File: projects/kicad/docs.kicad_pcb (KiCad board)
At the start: 2 copper layers, 2 parts

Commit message: Update_0122
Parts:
- added D1: D, kbd_parts:D_SOD-123-Pretty, F.Cu at (223.8, 55.4)
- added D2: D, kbd_parts:D_SOD-123-Pretty, F.Cu at (223.8, 58.8)
- added D3: D, kbd_parts:D_SOD-123-Pretty, F.Cu at (223.8, 62.1)
- added D4: D, kbd_parts:D_SOD-123-Pretty, F.Cu at (223.8, 65.5)
- added D5: D, kbd_parts:D_SOD-123-Pretty, F.Cu at (223.8, 68.8)
- added D6: D, kbd_parts:D_SOD-123-Pretty, F.Cu at (223.8, 72.2)
- added D7: D, kbd_parts:D_SOD-123-Pretty, F.Cu at (223.8, 75.5)
- added SW1: SW_PUSH, kbd:keyswitch_choc12_gateron_low_profile_hotswap_1u_no_led, F.Cu at (188.4, 44.1)
- added SW2: SW_PUSH, kbd:keyswitch_choc12_gateron_low_profile_hotswap_1u_no_led, F.Cu at (188.4, 53.4)
- added SW3: SW_PUSH, kbd:keyswitch_choc12_gateron_low_profile_hotswap_1u_no_led, F.Cu at (188.4, 62.7)
- added SW4: SW_PUSH, kbd:keyswitch_choc12_gateron_low_profile_hotswap_1u_no_led, F.Cu at (188.4, 72.0)
- added SW5: SW_PUSH, kbd:keyswitch_choc12_gateron_low_profile_hotswap_1u_no_led, F.Cu at (188.4, 81.2)
- added SW6: SW_PUSH, kbd:keyswitch_choc12_gateron_low_profile_hotswap_1u_no_led, F.Cu at (188.4, 90.5)
- added SW7: RotaryEncoder_Switch, Rotary_Encoder:RotaryEncoder_Bourns_Vertical_PEC12R-3x17F-Sxxxx, F.Cu at (186.5, 119.5)
- added U2: LCD, ST7789v_Library:ST7789V, F.Cu at (98.8, 109.3)

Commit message: chocolate: Update_0126
とりあえず部品の配置。
配線はまだ手つけてないです。。
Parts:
- removed the REF** at (126.0, 46.5)
- added D10: LED, kbd:LED_WS2812B-PLCC4, F.Cu at (186.0, 108.0)
- added D8: LED, kbd:LED_WS2812B-PLCC4, F.Cu at (167.0, 108.0)
- added D9: LED, kbd:LED_WS2812B-PLCC4, F.Cu at (176.5, 108.0)
- D1, D2, D3, D4, D5, D6, D7, SW1, SW2, SW3, SW4, SW5, SW6, SW7: moved to B.Cu
- moved D2 129.5 mm to (105.3, 111.0), turned to 180 degrees
- moved D1 119.8 mm to (105.0, 70.5), turned to 180 degrees
- moved D4 109.3 mm to (124.5, 111.0), turned to 180 degrees
- moved D3 99.9 mm to (124.3, 70.5), turned to 180 degrees
- moved SW2 95.4 mm to (105.3, 100.2), turned to 180 degrees
- moved REF** 93.7 mm to (176.1, 51.9)
- moved SW1 91.0 mm to (105.2, 81.0), turned to 180 degrees
- moved D6 88.8 mm to (144.0, 111.0), turned to 180 degrees
- moved D5 80.1 mm to (143.8, 70.5), turned to 180 degrees
- moved U2 73.2 mm to (92.5, 36.3)
- moved SW4 70.0 mm to (124.4, 100.2), turned to 180 degrees
- moved SW3 66.6 mm to (124.4, 81.0), turned to 180 degrees
- moved D7 53.3 mm to (176.2, 99.5), turned to 180 degrees
- moved SW6 46.0 mm to (143.5, 100.2), turned to 180 degrees
- moved SW5 44.9 mm to (143.5, 81.0), turned to 180 degrees
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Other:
- board outline added: 107 x 89.5 mm

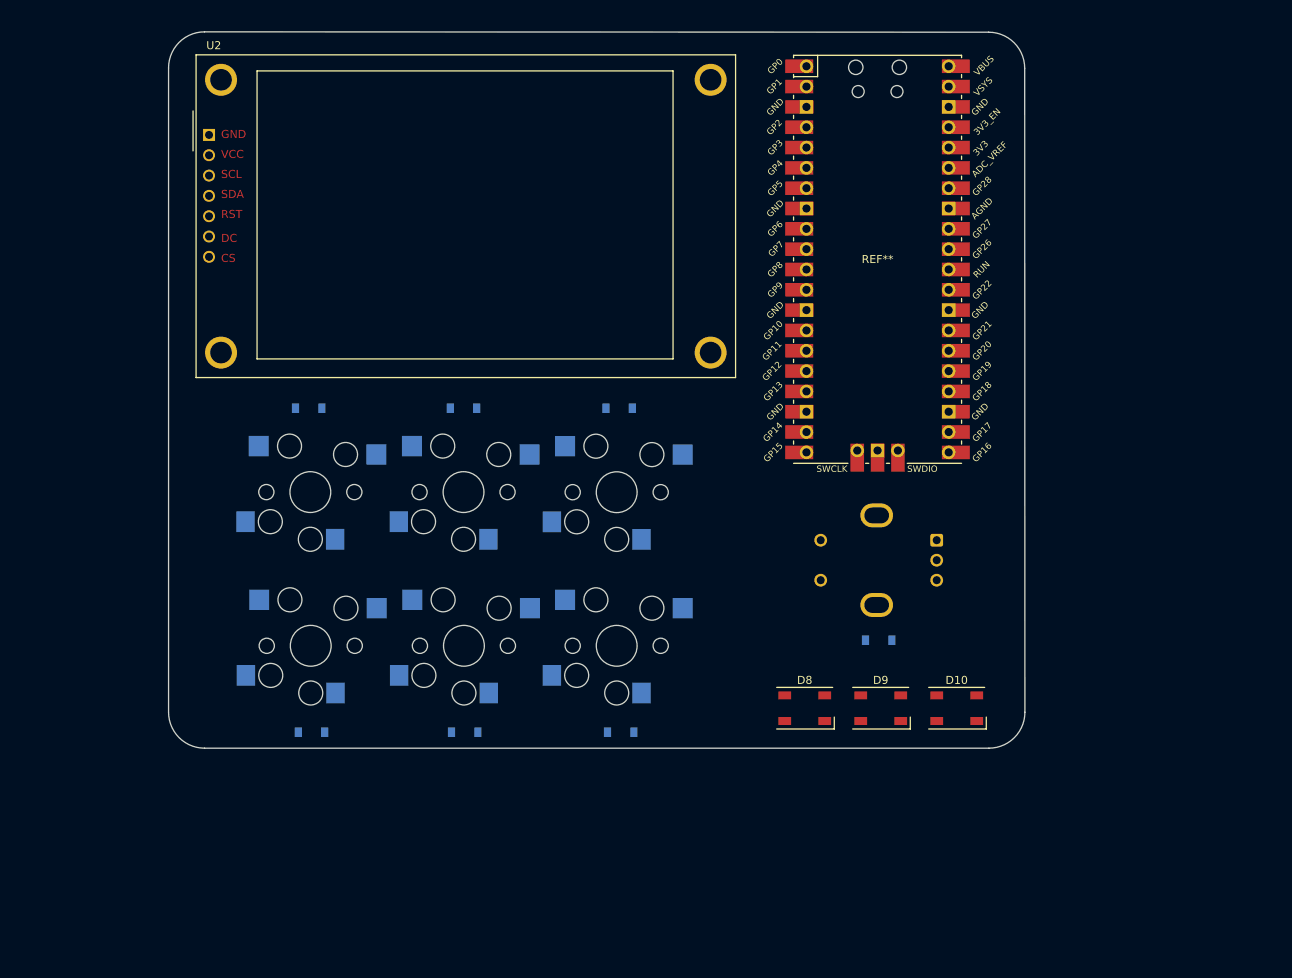
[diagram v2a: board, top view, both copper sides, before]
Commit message: chocolate: Update_0126
TFTディスプレイ 240x320 追加
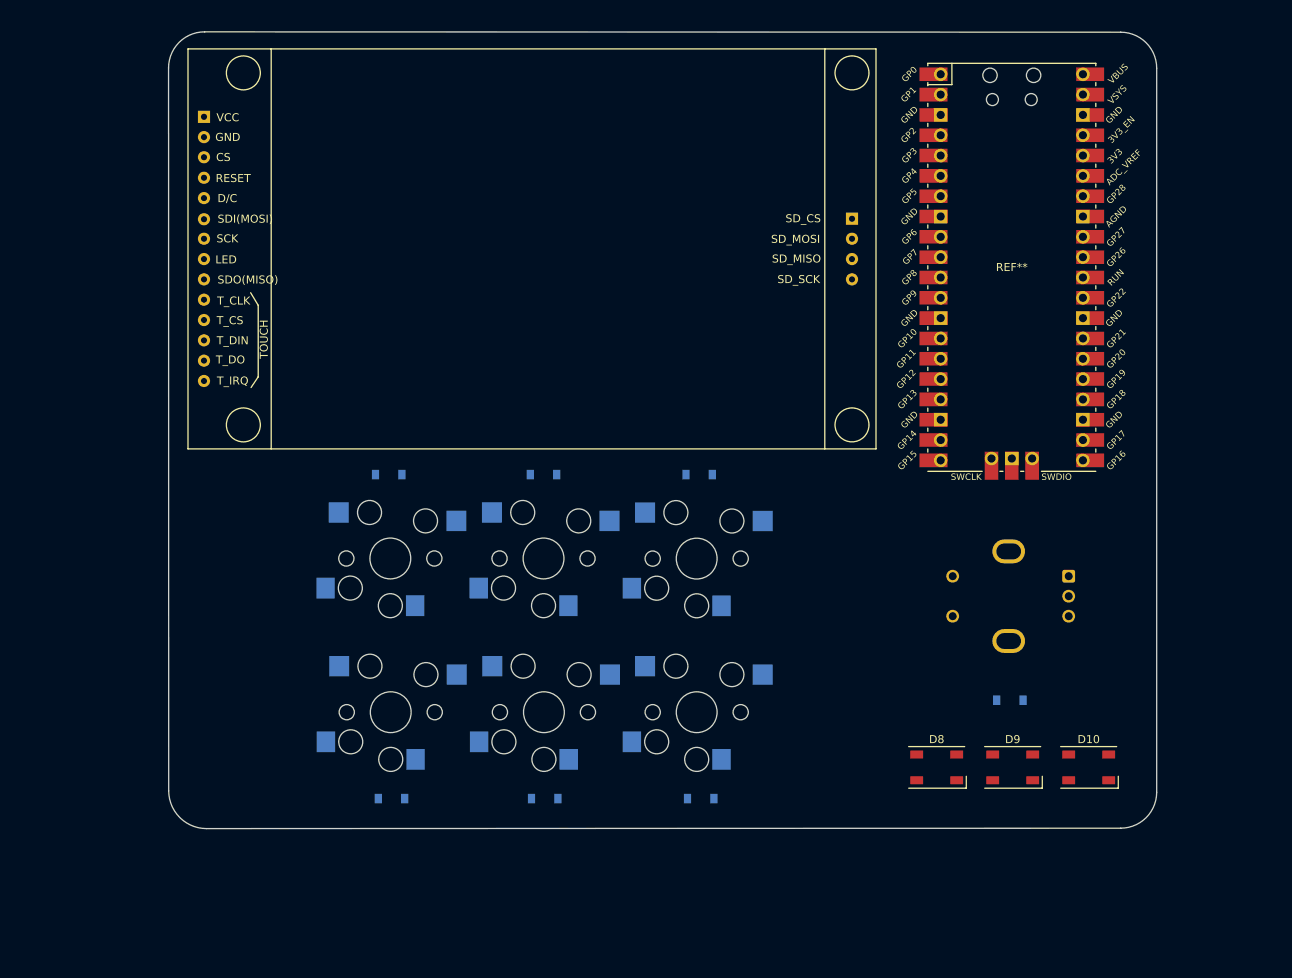
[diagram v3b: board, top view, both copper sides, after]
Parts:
- U2: footprint ST7789v_Library:ST7789V -> tft_displays:2.8_tft_240x320_touch_sd_spi
- moved U2 84.1 mm to (175.9, 25.6), turned to -90 degrees
- moved D10 18.1 mm to (202.5, 115.4)
- moved D8 18.1 mm to (183.5, 115.4)
- moved D9 18.1 mm to (193.0, 115.4)
- moved D7 18.0 mm to (192.7, 107.0)
- moved SW7 17.1 mm to (200.0, 91.5)
- moved REF** 16.8 mm to (192.9, 52.9)
- moved D1 13.0 mm to (115.0, 78.8)
- moved D2 13.0 mm to (115.3, 119.3)
- moved D3 13.0 mm to (134.3, 78.8)
- moved D4 13.0 mm to (134.5, 119.3)
- moved D5 13.0 mm to (153.8, 78.8)
- moved D6 13.0 mm to (154.0, 119.3)
- moved SW1 13.0 mm to (115.2, 89.3)
- moved SW2 13.0 mm to (115.3, 108.5)
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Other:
- board size 107 x 89.5 mm -> 123.5 x 99.6 mm

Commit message: Update_0128
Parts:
- removed REF**: RPi_Pico_SMD_TH, KiCAD_RP_Pico:RPi_Pico_SMD_TH
- removed U2: LCD, tft_displays:2.8_tft_240x320_touch_sd_spi
- added U1: Pico, KiCad-RP-Pico-main:RPi_Pico_SMD_TH, F.Cu at (149.4, 39.4)
- added U3: 2.8_240x320_touch_sd_spi, original_tft_display:2.8_tft_240x320_touch_sd_spi, F.Cu at (176.0, 24.0)
- moved D10 33.4 mm to (170.0, 107.5)
- moved D9 32.0 mm to (162.0, 107.5)
- moved D7 31.2 mm to (161.9, 101.5)
- moved SW7 31.2 mm to (169.2, 86.0)
- moved D8 30.5 mm to (154.0, 107.5)
- moved D1 16.0 mm to (99.0, 78.0)
- moved D2 16.0 mm to (99.3, 118.5)
- moved D3 16.0 mm to (118.3, 78.0)
- moved D4 16.0 mm to (118.5, 118.5)
- moved D5 16.0 mm to (137.8, 78.0)
- moved D6 16.0 mm to (138.0, 118.5)
- moved SW1 16.0 mm to (99.2, 88.5)
- moved SW2 16.0 mm to (99.3, 107.7)
- moved SW3 16.0 mm to (118.4, 88.5)
- moved SW4 16.0 mm to (118.4, 107.7)
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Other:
- board size 123.5 x 99.6 mm -> 96.5 x 103.5 mm

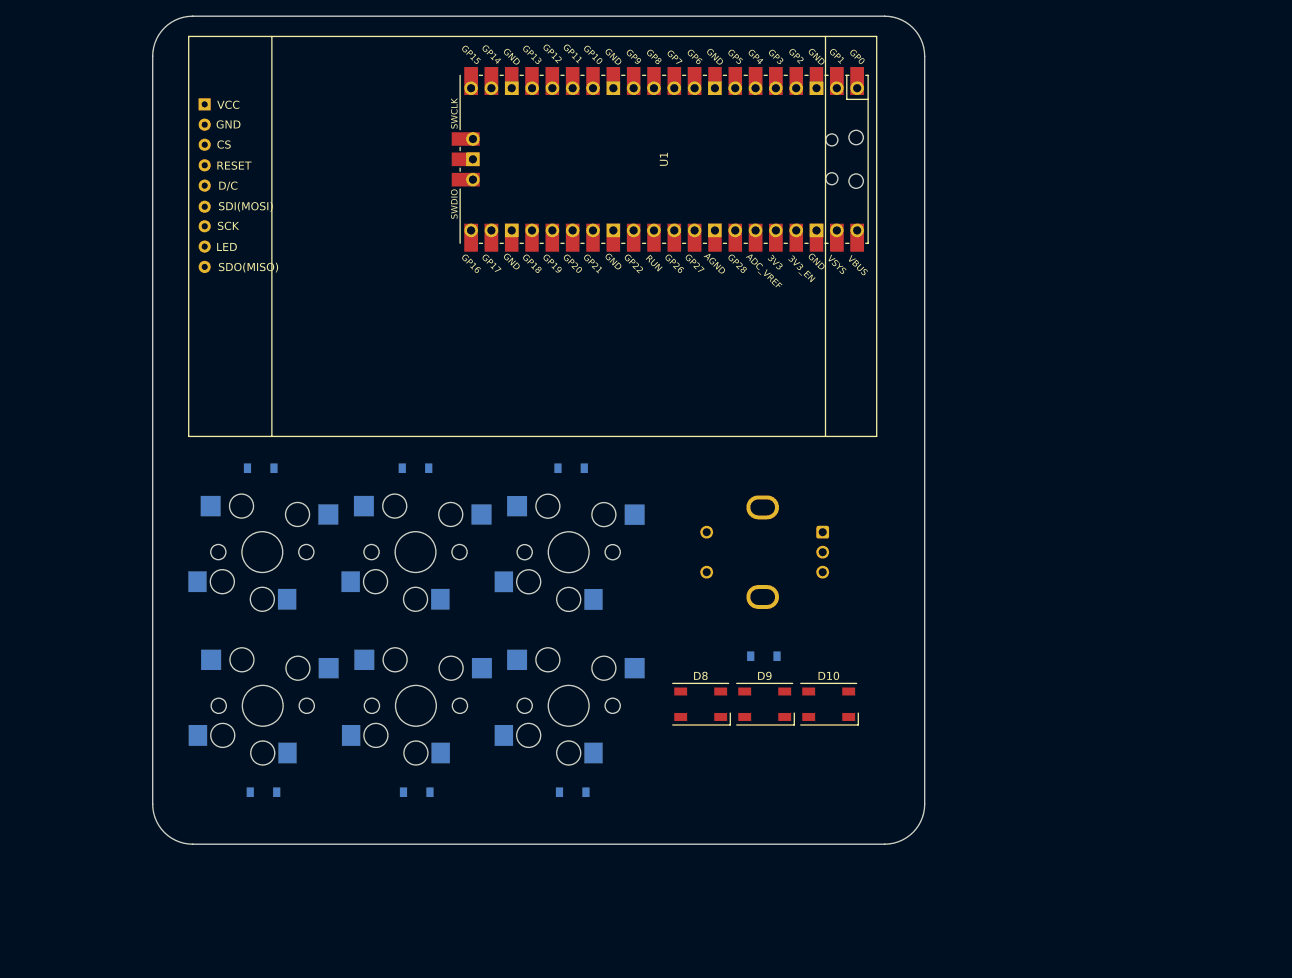
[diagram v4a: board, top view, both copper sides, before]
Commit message: chocolate: Update 01_29
配線を実施。
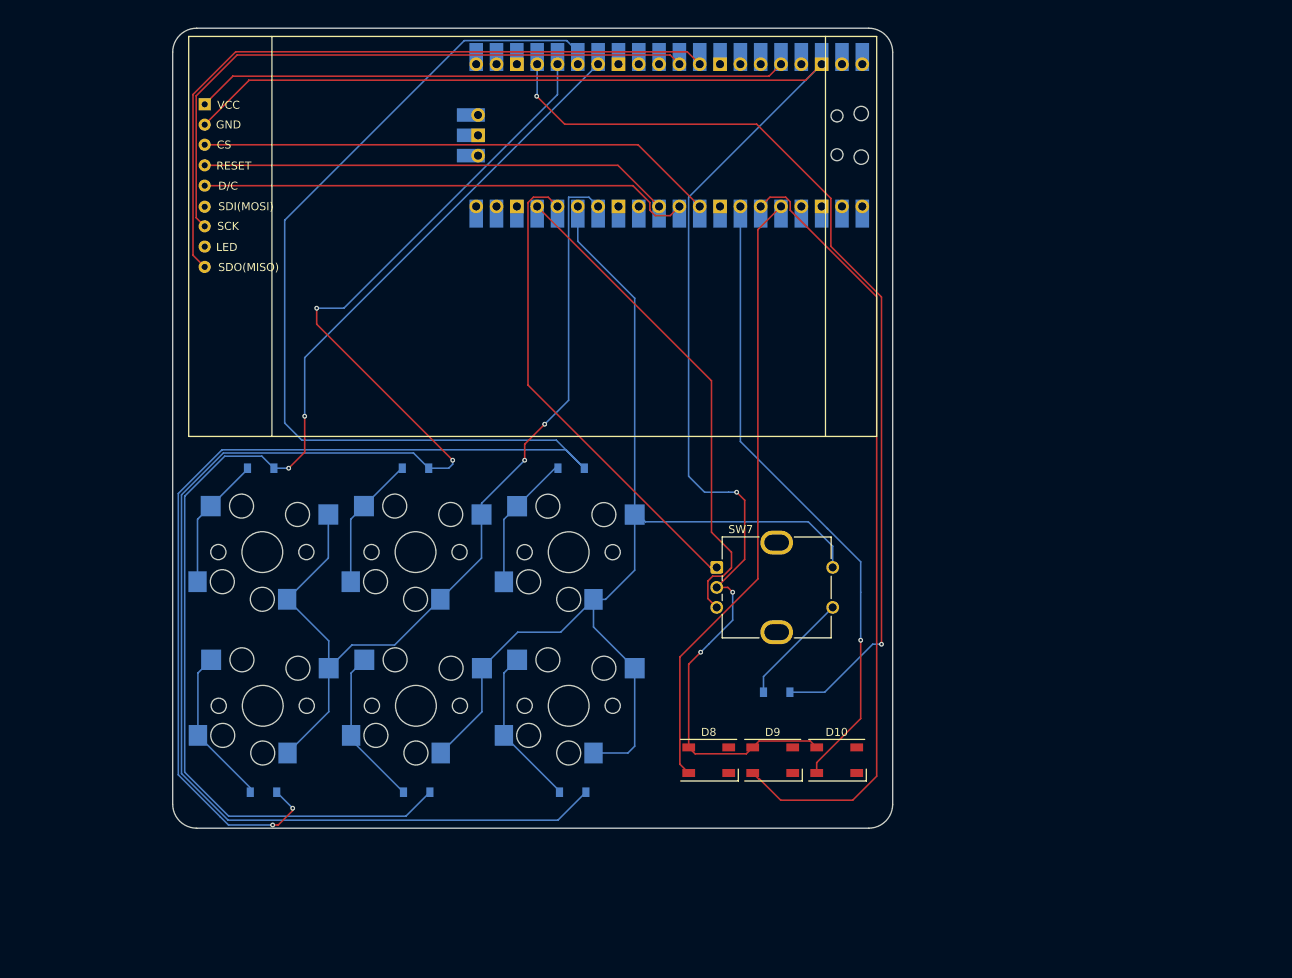
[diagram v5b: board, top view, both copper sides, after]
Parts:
- SW7: moved to F.Cu
- U1: moved to B.Cu
- moved SW7 14.0 mm to (156.0, 90.4), turned to 0 degrees
- moved D10 7.07 mm to (171.0, 114.5)
- moved D8 7.07 mm to (155.0, 114.5)
- moved D9 7.07 mm to (163.0, 114.5)
- moved D7 4.78 mm to (163.5, 106.0)
- moved U1 3.07 mm to (150.1, 36.4), turned to 90 degrees
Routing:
- net Row1: track 0.00 -> 223.1 mm, vias 0 -> 2
- net GND: track 0.00 -> 200.5 mm, vias 0 -> 3
- net Row2: track 0.00 -> 197.8 mm, vias 0 -> 2
- net Row0: track 0.00 -> 150.9 mm, vias 0 -> 2
- net Cal1: track 0.00 -> 140.4 mm
- net Row3: track 0.00 -> 118.4 mm, vias 0 -> 2
- net Cal0: track 0.00 -> 114.8 mm, vias 0 -> 2
- net Net-(D9-A): track 0.00 -> 100.6 mm
- net SDA: track 0.00 -> 88.4 mm
- net SCL: track 0.00 -> 79.7 mm
- net Net-(D10-A): track 0.00 -> 79.3 mm, vias 0 -> 1
- net Net-(D8-A): track 0.00 -> 77.2 mm
- net 3V3 Out: track 0.00 -> 74.1 mm
- net CS: track 0.00 -> 65.1 mm
- net RE_B: track 0.00 -> 62.6 mm
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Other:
- board size 96.5 x 103.5 mm -> 90 x 100 mm

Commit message: Update_0129
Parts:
- removed D10, D8, D9: LED, kbd:LED_WS2812B-PLCC4
- added LED1: YS-SK6812MINI-E, kbd:YS-SK6812MINI-E, F.Cu at (155.5, 112.0)
- added LED2: YS-SK6812MINI-E, kbd:YS-SK6812MINI-E, F.Cu at (163.5, 112.0)
- added LED3: YS-SK6812MINI-E, kbd:YS-SK6812MINI-E, F.Cu at (172.0, 112.0)
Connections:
- U1 pad 31: SCL -> SDA
- U1 pad 32: SDA -> SCL
- U1 pad 5: Net-(D8-A) -> LED
- U1 pad 6: Net-(D9-A) -> unconnected-(U1-GPIO4-Pad6)
- U1 pad 7: Net-(D10-A) -> unconnected-(U1-GPIO5-Pad7)
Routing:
- net 3V3 Out: track 74.1 -> 202.8 mm, vias 0 -> 1
- net Net-(D9-A): track 100.6 -> 0.00 mm
- net Net-(D10-A): track 79.3 -> 0.00 mm, vias 1 -> 0
- net Net-(D8-A): track 77.2 -> 0.00 mm
- net LED: track 0.00 -> 71.4 mm
- net SCL: track 79.7 -> 89.9 mm
- net SDA: track 88.4 -> 92.4 mm
- net Net-(LED1-DOUT): track 0.00 -> 4.04 mm
- net Net-(LED2-DOUT): track 0.00 -> 3.48 mm
- net GND: track 200.5 -> 203.0 mm, vias 3 -> 1
- net unconnected-(U1-GPIO4-Pad6): track 0.00 -> 1.72 mm
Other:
- board text added: "ShowaIntelligence"

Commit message: Update_0129_yamaguchi
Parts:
- moved U1 2.72 mm to (150.2, 39.1)
- moved LED1 1.20 mm to (154.3, 112.0)
- moved LED3 0.30 mm to (172.3, 112.0)
- moved LED2 0.20 mm to (163.3, 112.0)
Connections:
- U1 pad 10: DC -> RE_B
- U1 pad 11: RST -> LED
- U1 pad 12: unconnected-(U1-GPIO9-Pad12) -> Cal1
- U1 pad 14: Cal0 -> Row1
- U1 pad 15: Cal1 -> Cal0
- U1 pad 16: RE_A -> Row2
- U1 pad 17: RE_B -> Row0
- U1 pad 24: Row3 -> unconnected-(U1-GPIO18-Pad24)
- U1 pad 25: Row2 -> DC
- U1 pad 26: Row1 -> RST
- U1 pad 27: Row0 -> CS
- U1 pad 5: LED -> Row3
- U1 pad 9: CS -> RE_A
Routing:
- net Row1: track 223.1 -> 106.3 mm
- net Row2: track 197.8 -> 111.5 mm
- net GND: track 203.0 -> 275.8 mm
- net Row3: track 118.4 -> 67.9 mm, vias 2 -> 0
- net SDA: track 92.4 -> 69.8 mm
- net RE_A: track 60.3 -> 44.5 mm
- net Row0: track 150.9 -> 135.1 mm, vias 2 -> 0
- net SCL: track 89.9 -> 74.2 mm
- net Cal1: track 140.4 -> 155.4 mm
- net RE_B: track 62.6 -> 49.3 mm
- net DC: track 61.9 -> 50.3 mm
- net Cal0: track 114.8 -> 107.6 mm, vias 2 -> 0
- net LED: track 71.4 -> 64.6 mm
- net CS: track 65.1 -> 59.3 mm
- net RST: track 58.9 -> 54.9 mm
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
